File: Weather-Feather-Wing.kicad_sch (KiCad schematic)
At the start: 35 parts, among them J2 Conn_01x16, J3 Conn_01x12, Q1 BSS138, U1 AP2112K-3.3, U2 SHT4x, U3 SCD41-D-R2, U4 BMP390, U5 SGP40-D-R4

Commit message: Corrections and improvements.
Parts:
- C8, C9: value 0.1uF -> 1uF
- R7: value 10K -> 4.7
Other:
- note added: "Check schematic in Section 2.5 Interface Specifications of the datasheet."
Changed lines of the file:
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@@
 	(generator_version "9.0")
 	(paper "USLedger")
+	(text "Check schematic in Section 2.5 Interface Specifications of the datasheet."
+		(exclude_from_sim no)
+		(at 288.036 147.828 0)
+		(effects
+			(font
+				(size 1.27 1.27)
+			)
+		)
+	)
 	(text "ON LED"
 		(exclude_from_sim no)
@@
 			)
 		)
-		(property "Value" "0.1uF"
+		(property "Value" "1uF"
 			(at 323.85 177.7999 0)
 			(effects
@@
 			)
 		)
-		(property "Value" "0.1uF"
+		(property "Value" "1uF"
 			(at 309.88 185.4199 0)
 			(effects
@@
 			)
 		)
-		(property "Value" "10K"
+		(property "Value" "4.7"
 			(at 322.58 167.6399 0)
 			(effects

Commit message: As ordered from OSH Park.
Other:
- note added: "VDD: 1.65V - 3.6V TEMPERATURE: -40*C - 85*C I2C ADDRESS: 0x77 BMP581 I2C Address: 0x47"
- note removed: "VDD: 1.65V - 3.6V TEMPERATURE: -40*C - 85*C I2C ADDRESS: 0x77"
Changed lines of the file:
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@@
 		)
 	)
-	(text "VDD: 1.65V - 3.6V\nTEMPERATURE: -40*C - 85*C\nI2C ADDRESS: 0x77"
+	(text "VDD: 1.65V - 3.6V\nTEMPERATURE: -40*C - 85*C\nI2C ADDRESS: 0x77\n\nBMP581 I2C Address: 0x47"
 		(exclude_from_sim no)
 		(at 69.85 228.6 0)

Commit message: Cleanup and updates
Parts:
- removed CONN1, CONN2: STEMMA_I2C_QT, Adafruit SHT45:JST_SH4, symbol Adafruit SHT45-eagle-import:STEMMA_I2C_QT
- added J5, J6: JST_SH4, Weather_Feather:JST_SH4, symbol TI_MSPM0:QWIIC
- H1, H2, H3, H4: footprint Adafruit BMP390:FEATHER_MOUNTING_HOLE_2.5_PLATED -> TI_MSPM0_DSBGA:MOUNTINGHOLE_2.5_PLATED
- U2: footprint Adafruit SHT45:SHT4X -> Weather_Feather:SHT4X
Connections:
- net GND: now also J5.1 (GND), J5.MT1 (MT), J5.MT2 (MT), J6.1 (GND), J6.MT1 (MT), J6.MT2 (MT)
- net SCL: now also J5.4 (SCL), J6.4 (SCL)
- net SDA: now also J5.3 (SDA), J6.3 (SDA)
- net VCC: now also J5.2 (VCC), J6.2 (VCC)
- net SCK_Feather: now reaches J2.11 (Pin_11)
- net MO_Feather: now reaches J2.12 (Pin_12)
- net MI_Feather: now reaches J2.13 (Pin_13)
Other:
- note added: "Add Isolation Jumpers for SPI connections to the Feather headers."
- note added: "Can be powered by 5V. Add isolation jumpers similiar to the Adafruit breakout board."
- note added: "I2C Pullups & Level Shifter"
- note added: "STEMMA /QWIIC /I2C Headers /JST SH"
- note added: "TO DO: Try the footprint cleanup wizard for the SHT4x and JST SH4 footprints."
- note removed: "I2C Pullups & Shift"
- note removed: "STEMMA/I2C Headers"
- note removed: "TO DO: Check LDO ripple AP2112K-3.3 Check max current consumption. Update to Ultra Librarian Schematic Symbols and Footprints. Check Datasheets and Adafruit Schematics Check recommended footprints in datasheets. Are there keepouts? Get Step Files Add I2C Addresses to the silkscreen on the back of the board. Try laying out the board in two layers with 4 square inches. Round the corners of the boar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"

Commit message: Updates after building the board.
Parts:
- removed D1: GREEN, Adafruit SHT45:CHIPLED_0603_NOOUTLINE, symbol Adafruit SHT45-eagle-import:LED0603_NOOUTLINE
- removed U1: AP2112K-3.3, Adafruit SHT45:SOT23-5, symbol Adafruit SHT45-eagle-import:VREG_SOT23-5
- added D1: GREEN, LED_SMD:LED_0603_1608Metric_Pad1.05x0.95mm_HandSolder, symbol Device:LED
- added U1: AP2112K-3.3, Weather_Feather:SOT23-5, symbol TI_MSPM0:AP2112K-3.3
- J1: renamed from J5; footprint Weather_Feather:JST_SH4 -> Weather_Feather:JST_SH_SM04B-SRSS-TB_1x04-1MP_P1.00mm_Horizontal
- J2: renamed from J6; footprint Weather_Feather:JST_SH4 -> Weather_Feather:JST_SH_SM04B-SRSS-TB_1x04-1MP_P1.00mm_Horizontal
- renumbered J2 to J3, J3 to J4
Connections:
- net +3.3V: now also U1.5 (VOUT)
- net GND: now also J1.MP1 (MP), J1.MP2 (MP), J2.MP1 (MP), J2.MP2 (MP), D1.1 (K), U1.2 (GND); no longer J1.MT1 (MT), J1.MT2 (MT), J2.MT1 (MT), J2.MT2 (MT)
- net VCC: now also U1.1 (VIN), U1.3 (EN)
- net at R1.2: now also D1.2 (A)
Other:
- note added: "CO2 + RH/T Sensor VDD: 2.4V - 5.5V IDD: 18 mA Max Typical Ipeak: 205 mA Max TEMPERATURE: -10°C - 60°C I2C ADDRESS: 0x62"
- note added: "FEATHER HEADERS"
- note added: "I2C PULLUPS & LEVEL SHIFTER"
- note added: "Indoor Air Quality Sensor VDD: 1.7V - 3.6V IDD: 3.0 mA Max. Average TEMPERATURE: -10°C - 50°C I2C ADDRESS: 0x59"
- note added: "MOUNTING HOLES"
- note added: "POWER SUPPLY"
- note added: "RH/T Sensor VDD: 1.1-3.6V IDD, HEATER OFF: 500 µA IDD, HEATER ON: 100 mA TEMPERATURE: -40°C - +125°C I2C ADDRESS: 0x44"
- note added: "VDD: 1.65V - 3.6V Ipeak: 730 µA TEMPERATURE: -40°C - +85°C I2C ADDRESS: 0x77 BMP581 I2C Address: 0x47"
- note added: "VIN: 6.0V Max VOUT: 3.3V IOUT: 600 mA Max TEMPERATURE: -40°C - +85°C"
- note removed: "Add Isolation Jumpers for SPI connections to the Feather headers."
- note removed: "CO2 + RH/T Sensor VDD: 2.4V - 5.5V I2C Address: 0x62"
- note removed: "Can be powered by 5V. Add isolation jumpers similiar to the Adafruit breakout board."
- note removed: "Check schematic in Section 2.5 Interface Specifications of the datasheet."
- note removed: "I2C ADDRESS: 0x59"
- note removed: "I2C Pullups & Level Shifter"
- note removed: "Power supply"
- note removed: "TO DO: Try the footprint cleanup wizard for the SHT4x and JST SH4 footprints."
- note removed: "VCC = 3.3V - 5.5V VBUS = 4.5V - 5.5V Connected to USB VBUS if installed on a Feather Board."
- note removed: "VDD: 1.1-3.6V Temperature: -40 - 125*C I2C ADDRESS: 0x44"
- note removed: "VDD: 1.65V - 3.6V TEMPERATURE: -40*C - 85*C I2C ADDRESS: 0x77 BMP581 I2C Address: 0x47"
- moved on the sheet: C1, C2, C3, C4, C5, C6, C7, C8, C9, J1, J2, J3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

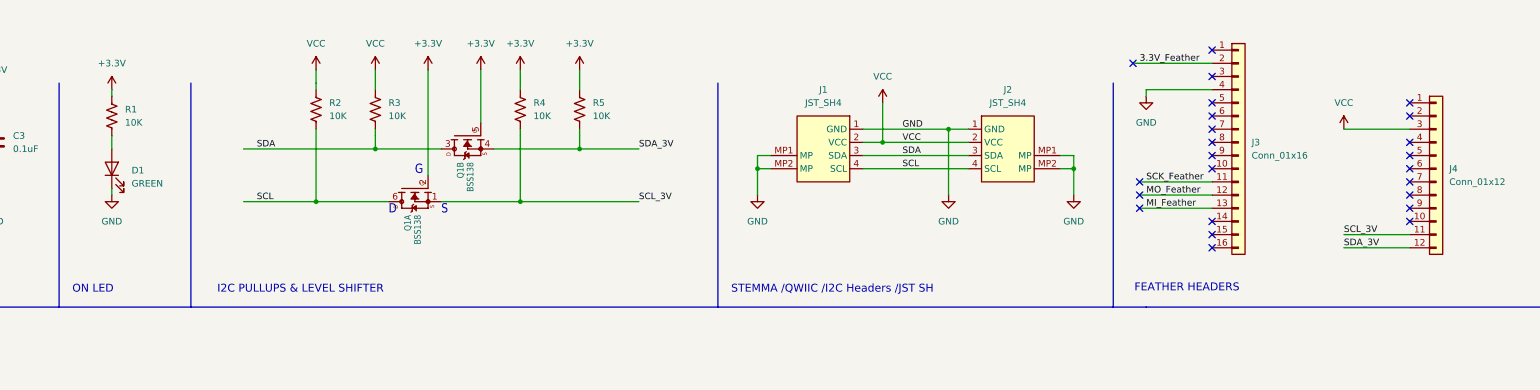
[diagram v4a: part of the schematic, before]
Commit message: Design corrections, moved both header pins 50 mils closer to their respective edges.
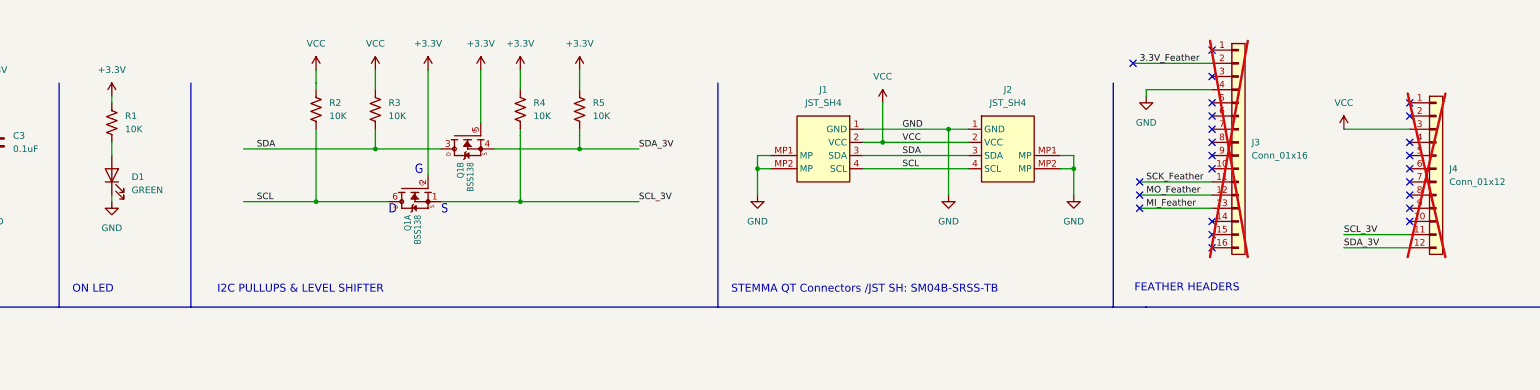
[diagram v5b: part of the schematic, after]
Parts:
- J3: footprint Connector_PinHeader_2.54mm:PinHeader_1x16_P2.54mm_Vertical -> Weather_Feather:PinHeader_1x16_P2.54mm_Vertical; now not fitted
- J4: footprint Connector_PinHeader_2.54mm:PinHeader_1x12_P2.54mm_Vertical -> Weather_Feather:PinHeader_1x12_P2.54mm_Vertical; now not fitted
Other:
- note added: "STEMMA QT Connectors /JST SH: SM04B-SRSS-TB"
- note removed: "STEMMA /QWIIC /I2C Headers /JST SH"
- moved on the sheet: D1, R1
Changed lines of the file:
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@@
 		)
 	)
-	(text "STEMMA /QWIIC /I2C Headers /JST SH"
+	(text "STEMMA QT Connectors /JST SH: SM04B-SRSS-TB"
 		(exclude_from_sim no)
 		(at 218.44 73.66 0)
@@
 	(wire
 		(pts
-			(xy 99.06 45.72) (xy 99.06 43.18)
+			(xy 99.06 46.99) (xy 99.06 44.45)
 		)
 		(stroke
@@
 	(wire
 		(pts
-			(xy 99.06 53.34) (xy 99.06 54.61)
+			(xy 99.06 54.61) (xy 99.06 55.88)
 		)
 		(stroke
@@
 	(wire
 		(pts
-			(xy 99.06 34.29) (xy 99.06 35.56)
+			(xy 99.06 35.56) (xy 99.06 36.83)
 		)
 		(stroke
@@
 	(symbol
 		(lib_id "power:GND")
-		(at 99.06 54.61 0)
+		(at 99.06 55.88 0)
 		(unit 1)
 		(exclude_from_sim no)
@@
 		(fields_autoplaced yes)
 		(property "Reference" "#PWR016"
-			(at 99.06 60.96 0)
+			(at 99.06 62.23 0)
 			(effects
 				(font
@@
 		)
 		(property "Value" "GND"
-			(at 99.06 59.69 0)
+			(at 99.06 60.96 0)
 			(effects
 				(font
@@
 		)
 		(property "Footprint" ""
-			(at 99.06 54.61 0)
+			(at 99.06 55.88 0)
 			(effects
 				(font
@@
 		)
 		(property "Datasheet" ""
-			(at 99.06 54.61 0)
+			(at 99.06 55.88 0)
 			(effects
 				(font
@@
 		)
 		(property "Description" "Power symbol creates a global label with name \"GND\" , ground"
-			(at 99.06 54.61 0)
+			(at 99.06 55.88 0)
 			(effects
 				(font
@@
 		(in_bom yes)
 		(on_board yes)
-		(dnp no)
+		(dnp yes)
 		(fields_autoplaced yes)
 		(property "Reference" "J3"
@@
 			)
 		)
-		(property "Footprint" "Connector_PinHeader_2.54mm:PinHeader_1x16_P2.54mm_Vertical"
+		(property "Footprint" "Weather_Feather:PinHeader_1x16_P2.54mm_Vertical"
 			(at 316.23 44.45 0)
 			(effects
@@
 	(symbol
 		(lib_id "power:+3.3V")
-		(at 99.06 34.29 0)
+		(at 99.06 35.56 0)
 		(unit 1)
 		(exclude_from_sim no)
@@
 		(fields_autoplaced yes)
 		(property "Reference" "#PWR011"
-			(at 99.06 38.1 0)
+			(at 99.06 39.37 0)
 			(effects
 				(font
@@
 		)
 		(property "Value" "+3.3V"
-			(at 99.06 29.21 0)
+			(at 99.06 30.48 0)
 			(effects
 				(font
@@
 		)
 		(property "Footprint" ""
-			(at 99.06 34.29 0)
+			(at 99.06 35.56 0)
 			(effects
 				(font
@@
 		)
 		(property "Datasheet" ""
-			(at 99.06 34.29 0)
+			(at 99.06 35.56 0)
 			(effects
 				(font
@@
 		)
 		(property "Description" "Power symbol creates a global label with name \"+3.3V\""
-			(at 99.06 34.29 0)
+			(at 99.06 35.56 0)
 			(effects
 				(font
@@
 	(symbol
 		(lib_id "Device:LED")
-		(at 99.06 49.53 90)
+		(at 99.06 50.8 90)
 		(unit 1)
 		(exclude_from_sim no)
@@
 		(fields_autoplaced yes)
 		(property "Reference" "D1"
-			(at 102.87 49.8474 90)
+			(at 102.87 51.1174 90)
 			(effects
 				(font
@@
 		)
 		(property "Value" "GREEN"
-			(at 102.87 52.3874 90)
+			(at 102.87 53.6574 90)
 			(effects
 				(font
@@
 		)
 		(property "Footprint" "LED_SMD:LED_0603_1608Metric_Pad1.05x0.95mm_HandSolder"
-			(at 99.06 49.53 0)
+			(at 99.06 50.8 0)
 			(effects
 				(font
@@
 		)
 		(property "Datasheet" "~"
-			(at 99.06 49.53 0)
+			(at 99.06 50.8 0)
 			(effects
 				(font
@@
 		)
 		(property "Description" "Light emitting diode"
-			(at 99.06 49.53 0)
+			(at 99.06 50.8 0)
 			(effects
 				(font
@@
 		)
 		(property "Sim.Pins" "1=K 2=A"
-			(at 99.06 49.53 0)
+			(at 99.06 50.8 0)
 			(effects
 				(font
@@
 	(symbol
 		(lib_id "Device:R_US")
-		(at 99.06 39.37 0)
+		(at 99.06 40.64 0)
 		(unit 1)
 		(exclude_from_sim no)
@@
 		(fields_autoplaced yes)
 		(property "Reference" "R1"
-			(at 101.6 38.0999 0)
+			(at 101.6 39.3699 0)
 			(effects
 				(font
@@
 		)
 		(property "Value" "10K"
-			(at 101.6 40.6399 0)
+			(at 101.6 41.9099 0)
 			(effects
 				(font
@@
 		)
 		(property "Footprint" "Resistor_SMD:R_0603_1608Metric_Pad0.98x0.95mm_HandSolder"
-			(at 100.076 39.624 90)
+			(at 100.076 40.894 90)
 			(effects
 				(font
@@
 		)
 		(property "Datasheet" "~"
-			(at 99.06 39.37 0)
+			(at 99.06 40.64 0)
 			(effects
 				(font
@@
 		)
 		(property "Description" "Resistor, US symbol"
-			(at 99.06 39.37 0)
+			(at 99.06 40.64 0)
 			(effects
 				(font
@@
 		(in_bom yes)
 		(on_board yes)
-		(dnp no)
+		(dnp yes)
 		(fields_autoplaced yes)
 		(property "Reference" "J4"
@@
 			)
 		)
-		(property "Footprint" "Connector_PinHeader_2.54mm:PinHeader_1x12_P2.54mm_Vertical"
+		(property "Footprint" "Weather_Feather:PinHeader_1x12_P2.54mm_Vertical"
 			(at 354.33 49.53 0)
 			(effects
